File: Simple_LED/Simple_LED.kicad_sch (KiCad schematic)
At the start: 3 parts

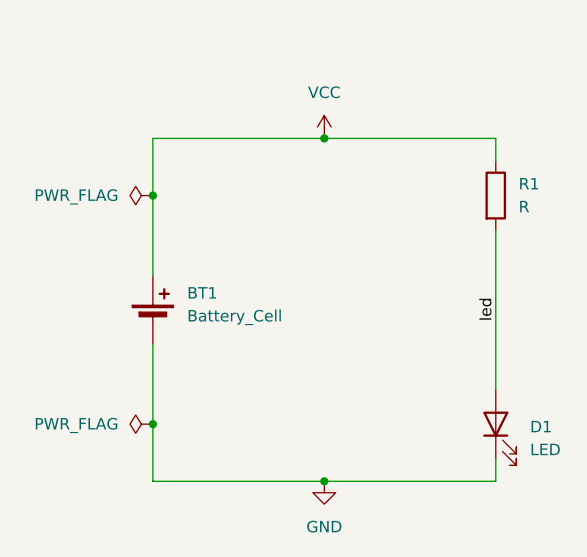
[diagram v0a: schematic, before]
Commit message: Add 4bits adder
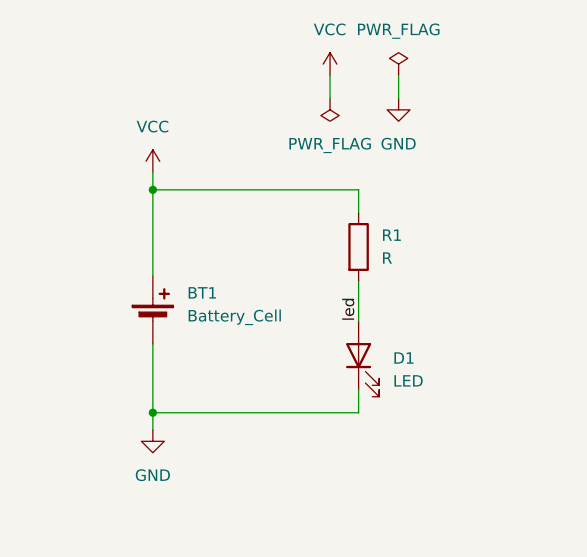
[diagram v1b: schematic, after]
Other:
- moved on the sheet: D1, R1
